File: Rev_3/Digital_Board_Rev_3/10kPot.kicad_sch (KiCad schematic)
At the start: 2 parts

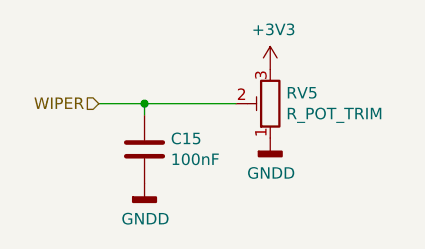
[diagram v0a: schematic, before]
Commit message: Pivoting to Passive Jack Boards
Finalized layout for input/output Jack Boards, which are now completely passive and connected with board-to-board connectors. Schematics are not updated yet, just figuring out placement/dimensions.
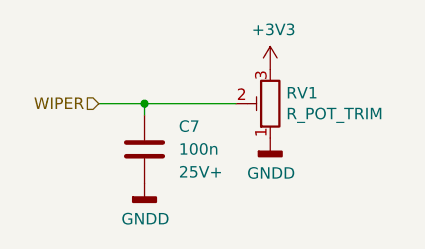
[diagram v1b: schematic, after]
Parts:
- removed C15: 100nF, Capacitor_SMD:C_0805_2012Metric_Pad1.18x1.45mm_HandSolder, symbol Device:C
- added C7: 100n, Capacitor_SMD:C_0402_1005Metric, symbol #gplm:cap/RES-4003-100N
- renumbered RV5 to RV1
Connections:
- net GNDD: now also C7.2
- net WIPER: now also C7.1
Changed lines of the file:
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@@
 		(on_board yes)
 		(dnp no)
-		(property "Reference" "RV5"
+		(property "Reference" "RV1"
 			(at 127.508 94.0816 0)
 			(effects
@@
 				(path "/961bce4d-0f15-4753-8332-e4f92c717c57/00000000-0000-0000-0000-0000603bfce9"
 					(reference "RV5")
-					(unit 1)
-				)
-				(path "/961bce4d-0f15-4753-8332-e4f92c717c57/00000000-0000-0000-0000-00006052a5b7"
-					(reference "RV10")
 					(unit 1)
 				)
@@
 		(on_board yes)
 		(dnp no)
-		(property "Reference" "#PWR0122"
+		(property "Reference" "#PWR0110"
 			(at 125.73 105.41 0)
 			(effects
@@
 				(path "/961bce4d-0f15-4753-8332-e4f92c717c57/00000000-0000-0000-0000-0000603bfce9"
 					(reference "#PWR0122")
-					(unit 1)
-				)
-				(path "/961bce4d-0f15-4753-8332-e4f92c717c57/00000000-0000-0000-0000-00006052a5b7"
-					(reference "#PWR0128")
 					(unit 1)
 				)
@@
 		(on_board yes)
 		(dnp no)
-		(property "Reference" "#PWR0123"
+		(property "Reference" "#PWR0111"
 			(at 125.73 95.25 0)
 			(effects
@@
 				(path "/961bce4d-0f15-4753-8332-e4f92c717c57/00000000-0000-0000-0000-0000603bfce9"
 					(reference "#PWR0123")
-					(unit 1)
-				)
-				(path "/961bce4d-0f15-4753-8332-e4f92c717c57/00000000-0000-0000-0000-00006052a5b7"
-					(reference "#PWR0126")
-					(unit 1)
-				)
-			)
-		)
-	)
-	(symbol
-		(lib_id "Device:C")
-		(at 111.76 100.33 0)
-		(unit 1)
-		(exclude_from_sim no)
-		(in_bom yes)
-		(on_board yes)
-		(dnp no)
-		(property "Reference" "C15"
-			(at 114.681 99.1616 0)
-			(effects
-				(font
-					(size 1.27 1.27)
-				)
-				(justify left)
-			)
-		)
-		(property "Value" "100nF"
-			(at 114.681 101.473 0)
-			(effects
-				(font
-					(size 1.27 1.27)
-				)
-				(justify left)
-			)
-		)
-		(property "Footprint" "Capacitor_SMD:C_0805_2012Metric_Pad1.18x1.45mm_HandSolder"
-			(at 112.7252 104.14 0)
-			(effects
-				(font
-					(size 1.27 1.27)
-				)
-				(hide yes)
-			)
-		)
-		(property "Datasheet" "~"
-			(at 111.76 100.33 0)
-			(effects
-				(font
-					(size 1.27 1.27)
-				)
-				(hide yes)
-			)
-		)
-		(property "Description" ""
-			(at 111.76 100.33 0)
-			(effects
-				(font
-					(size 1.27 1.27)
-				)
-				(hide yes)
-			)
-		)
-		(pin "1"
-		)
-		(pin "2"
-		)
-		(instances
-			(project ""
-				(path "/961bce4d-0f15-4753-8332-e4f92c717c57/00000000-0000-0000-0000-0000603af413"
-					(reference "C11")
-					(unit 1)
-				)
-				(path "/961bce4d-0f15-4753-8332-e4f92c717c57/00000000-0000-0000-0000-0000603b6e16"
-					(reference "C12")
-					(unit 1)
-				)
-				(path "/961bce4d-0f15-4753-8332-e4f92c717c57/00000000-0000-0000-0000-0000603b89d8"
-					(reference "C13")
-					(unit 1)
-				)
-				(path "/961bce4d-0f15-4753-8332-e4f92c717c57/00000000-0000-0000-0000-0000603b89db"
-					(reference "C14")
-					(unit 1)
-				)
-				(path "/961bce4d-0f15-4753-8332-e4f92c717c57/00000000-0000-0000-0000-0000603bfce9"
-					(reference "C15")
-					(unit 1)
-				)
-				(path "/961bce4d-0f15-4753-8332-e4f92c717c57/00000000-0000-0000-0000-00006052a5b7"
-					(reference "C26")
 					(unit 1)
 				)
@@
 		(on_board yes)
 		(dnp no)
-		(property "Reference" "#PWR0124"
+		(property "Reference" "#PWR0112"
 			(at 111.76 110.49 0)
 			(effects
@@
 					(unit 1)
 				)
-				(path "/961bce4d-0f15-4753-8332-e4f92c717c57/00000000-0000-0000-0000-00006052a5b7"
-					(reference "#PWR0127")
-					(unit 1)
-				)
+			)
+		)
+	)
+	(symbol
+		(lib_id "#gplm:cap/RES-4003-100N")
+		(at 111.76 100.33 0)
+		(unit 1)
+		(exclude_from_sim no)
+		(in_bom yes)
+		(on_board yes)
+		(dnp no)
+		(fields_autoplaced yes)
+		(property "Reference" "C7"
+			(at 115.57 97.7899 0)
+			(effects
+				(font
+					(size 1.27 1.27)
+				)
+				(justify left)
+			)
+		)
+		(property "Value" "100n"
+			(at 112.395 102.87 0)
+			(effects
+				(font
+					(size 1.27 1.27)
+				)
+				(justify left)
+				(hide yes)
+			)
+		)
+		(property "Footprint" "Capacitor_SMD:C_0402_1005Metric"
+			(at 112.7252 104.14 0)
+			(effects
+				(font
+					(size 1.27 1.27)
+				)
+				(hide yes)
+			)
+		)
+		(property "Datasheet" ""
+			(at 111.76 100.33 0)
+			(effects
+				(font
+					(size 1.27 1.27)
+				)
+				(hide yes)
+			)
+		)
+		(property "Description" "CAP SMD 100nF 0402 25V+ X7R"
+			(at 111.76 100.33 0)
+			(effects
+				(font
+					(size 1.27 1.27)
+				)
+				(hide yes)
+			)
+		)
+		(property "IPN" "RES-4003-100N"
+			(at 111.76 100.33 0)
+			(effects
+				(font
+					(size 1.27 1.27)
+				)
+				(hide yes)
+			)
+		)
+		(property "Manufacturer" ""
+			(at 111.76 100.33 0)
+			(effects
+				(font
+					(size 1.27 1.27)
+				)
+				(hide yes)
+			)
+		)
+		(property "MPN" ""
+			(at 111.76 100.33 0)
+			(effects
+				(font
+					(size 1.27 1.27)
+				)
+				(hide yes)
+			)
+		)
+		(property "Capacitance" "100n"
+			(at 115.57 100.3299 0)
+			(effects
+				(font
+					(size 1.27 1.27)
+				)
+				(justify left)
+			)
+		)
+		(property "Voltage" "25V+"
+			(at 115.57 102.8699 0)
+			(effects
+				(font
+					(size 1.27 1.27)
+				)
+				(justify left)
+			)
+		)
+		(property "Material" "X7R"
+			(at 111.76 100.33 0)
+			(effects
+				(font
+					(size 1.27 1.27)
+				)
+				(hide yes)
+			)
+		)
+		(property "Tolerance" ""
+			(at 111.76 100.33 0)
+			(effects
+				(font
+					(size 1.27 1.27)
+				)
+				(hide yes)
+			)
+		)
+		(pin "2"
+		)
+		(pin "1"
+		)
+		(instances
+			(project "Digital_Board_Rev3"
+				(path "/961bce4d-0f15-4753-8332-e4f92c717c57/00000000-0000-0000-0000-0000603af413"
+					(reference "C7")
+					(unit 1)
+				)
+				(path "/961bce4d-0f15-4753-8332-e4f92c717c57/00000000-0000-0000-0000-0000603b6e16"
+					(reference "C8")
+					(unit 1)
+				)
+				(path "/961bce4d-0f15-4753-8332-e4f92c717c57/00000000-0000-0000-0000-0000603b89d8"
+					(reference "C9")
+					(unit 1)
+				)
+				(path "/961bce4d-0f15-4753-8332-e4f92c717c57/00000000-0000-0000-0000-0000603b89db"
+					(reference "C10")
+					(unit 1)
+				)
